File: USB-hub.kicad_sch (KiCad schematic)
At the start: 11 parts, among them U302 CH334P, Y900 Crystal_GND24

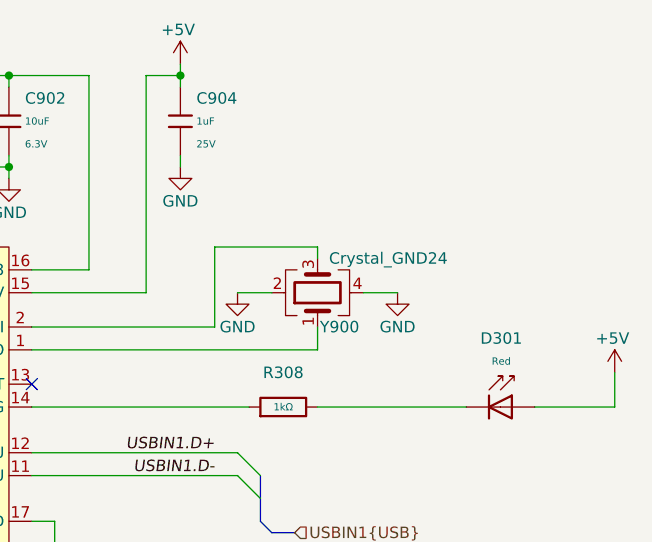
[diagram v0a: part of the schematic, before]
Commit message: [#8] Fix missing component values, fix soldermask expansion of U800 and remove its designator from silkscreen, minor schematic fixes
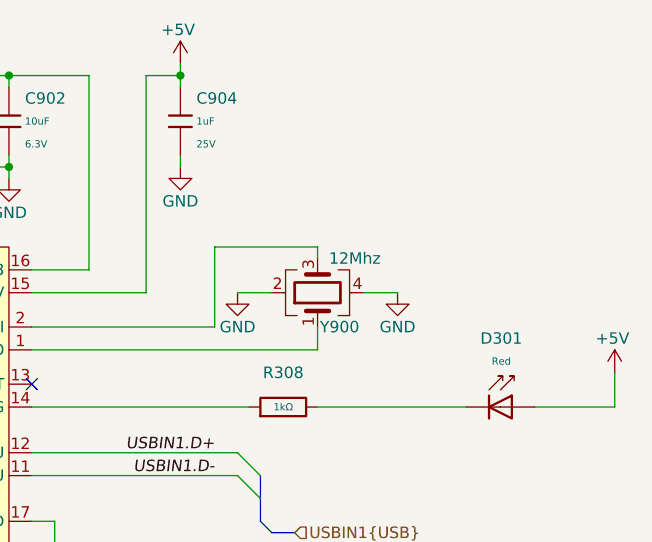
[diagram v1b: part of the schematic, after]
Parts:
- Y900: value Crystal_GND24 -> 12Mhz
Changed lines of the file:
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@@
+	)
+	(symbol
+		(lib_id "Device:Crystal_GND24")
+		(at 177.8 72.39 90)
+		(unit 1)
+		(exclude_from_sim no)
+		(in_bom yes)
+		(on_board yes)
+		(dnp no)
+		(property "Reference" "Y900"
+			(at 178.054 76.2 90)
+			(effects
+				(font
+					(size 1.27 1.27)
+				)
+				(justify right)
+			)
+		)
+		(property "Value" "12Mhz"
+			(at 179.07 68.58 90)
+			(effects
+				(font
+					(size 1.27 1.27)
+				)
+				(justify right)
+			)
+		)
+		(property "Footprint" "Crystal:Crystal_SMD_3225-4Pin_3.2x2.5mm"
+			(at 177.8 72.39 0)
+			(effects
+				(font
+					(size 1.27 1.27)
+				)
+				(hide yes)
+			)
+		)
+		(property "Datasheet" "~"
+			(at 177.8 72.39 0)
+			(effects
+				(font
+					(size 1.27 1.27)
+				)
+				(hide yes)
+			)
+		)
+		(property "Description" ""
+			(at 177.8 72.39 0)
+			(effects
+				(font
+					(size 1.27 1.27)
+				)
+				(hide yes)
+			)
+		)
+		(pin "1"
+		)
+		(pin "2"
+		)
+		(pin "3"
+		)
+		(pin "4"
+		)
+		(instances
+			(project "base-module"
+				(path "/090a8e41-87a8-4fb1-998b-60a2c0dc4cee/c4e62f69-aed8-45c4-bc74-414bd9b2dcad"
+					(reference "Y900")
+					(unit 1)
+				)
+			)
+		)
 	)
 	(symbol
@@
 					(unit 1)
 				)
-			)
-		)
-	)
-	(symbol
-		(lib_id "Device:Crystal_GND24")
-		(at 177.8 72.39 90)
-		(unit 1)
-		(exclude_from_sim no)
-		(in_bom yes)
-		(on_board yes)
-		(dnp no)
-		(property "Reference" "Y900"
-			(at 178.054 76.2 90)
-			(effects
-				(font
-					(size 1.27 1.27)
-				)
-				(justify right)
-			)
-		)
-		(property "Value" "Crystal_GND24"
-			(at 179.07 68.58 90)
-			(effects
-				(font
-					(size 1.27 1.27)
-				)
-				(justify right)
-			)
-		)
-		(property "Footprint" "Crystal:Crystal_SMD_3225-4Pin_3.2x2.5mm"
-			(at 177.8 72.39 0)
-			(effects
-				(font
-					(size 1.27 1.27)
-				)
-				(hide yes)
-			)
-		)
-		(property "Datasheet" "~"
-			(at 177.8 72.39 0)
-			(effects
-				(font
-					(size 1.27 1.27)
-				)
-				(hide yes)
-			)
-		)
-		(property "Description" "Four pin crystal, GND on pins 2 and 4"
-			(at 177.8 72.39 0)
-			(effects
-				(font
-					(size 1.27 1.27)
-				)
-				(hide yes)
-			)
-		)
-		(pin "1"
-		)
-		(pin "2"
-		)
-		(pin "3"
-		)
-		(pin "4"
-		)
-		(instances
-			(project "base-module"
-				(path "/090a8e41-87a8-4fb1-998b-60a2c0dc4cee/c4e62f69-aed8-45c4-bc74-414bd9b2dcad"
-					(reference "Y900")
-					(unit 1)
-				)

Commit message: [#1] Fill out schematic title block, connect GPIOs on the schematic
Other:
- title: ModuCard BM STM32H562VGT6 -> ModuCard GPIO module
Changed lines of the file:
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@@
 	(paper "A4")
 	(title_block
-		(title "ModuCard BM STM32H562VGT6")
-		(date "2025-04-18")
-		(rev "1.1.1")
+		(title "ModuCard GPIO module")
+		(date "2025-06-19")
+		(rev "1.0.0")
 		(company "KoNaR")
 		(comment 1 "Base project authors: Dominik Pluta, Artem Horiunov")
-		(comment 2 "Project author: <author>")
+		(comment 2 "Project author: Dominik Pluta")
 	)
 	(bus_alias "USB"
